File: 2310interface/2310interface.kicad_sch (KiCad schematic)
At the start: 63 parts, among them J4 Screw_Terminal_01x04, K1 Relay_SPDT, Q1 Q_NMOS_DSG, Q2 2N3904, SW1 SW_SPDT, U1 LD1117S50TR_SOT223

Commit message: Update after testing
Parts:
- C1: value C -> 100nF
- C2: value C -> 10uF
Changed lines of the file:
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@@
   )
   (symbol (lib_id "Device:R_US") (at 125.73 130.81 0) (unit 1)
-    (in_bom yes) (on_board yes) (dnp no) (fields_autoplaced)
-    (property "Reference" "R4" (at 128.27 129.54 0)
-      (effects (font (size 1.27 1.27)) (justify left))
-    )
-    (property "Value" "47K" (at 128.27 132.08 0)
+    (in_bom yes) (on_board yes) (dnp no)
+    (property "Reference" "R4" (at 121.92 130.81 0)
+      (effects (font (size 1.27 1.27)) (justify left))
+    )
+    (property "Value" "47K" (at 120.65 133.35 0)
       (effects (font (size 1.27 1.27)) (justify left))
     )
@@
       (effects (font (size 1.27 1.27)))
     )
-    (property "Value" "C" (at 194.31 88.9 90)
+    (property "Value" "10uF" (at 194.31 88.9 90)
       (effects (font (size 1.27 1.27)))
     )
@@
       (effects (font (size 1.27 1.27)))
     )
-    (property "Value" "C" (at 182.88 88.9 90)
-      (effects (font (size 1.27 1.27)))
-    )
+    (property "Value" "100nF" (at 182.88 88.9 90)
+      (effects (font (size 1.27 1.27)))
+    )

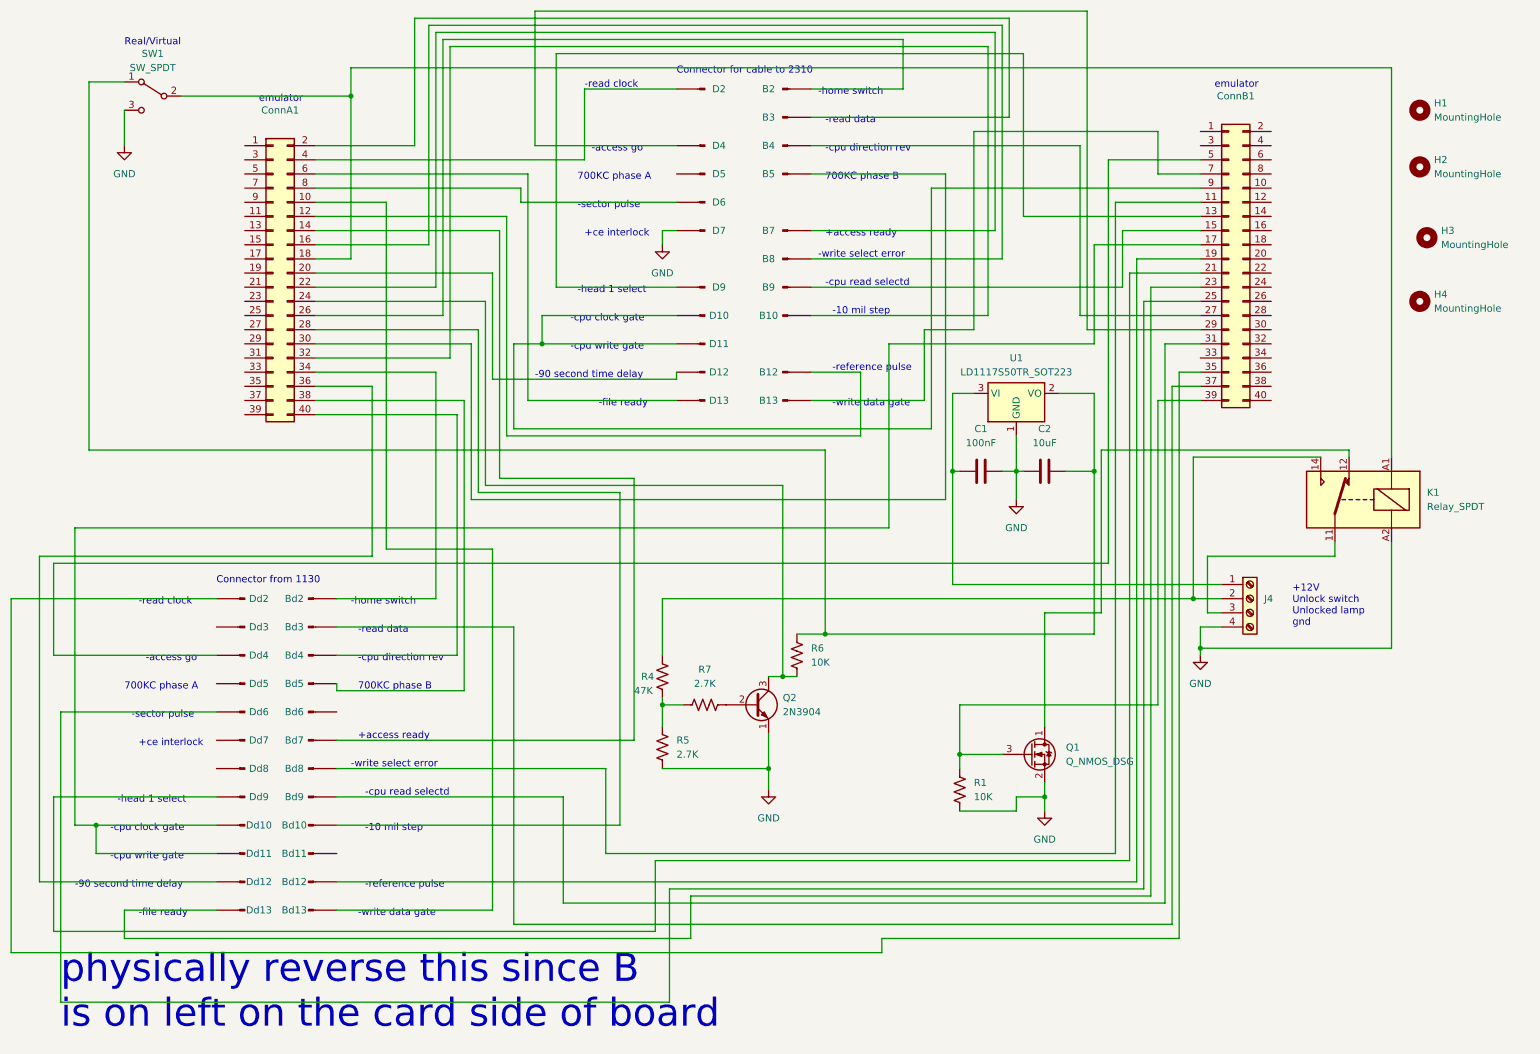
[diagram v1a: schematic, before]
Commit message: Fix defect in board
Inadvertent connection of +12V to the Unlock lamp driver
also increased current capacity for Unlock lamp traces
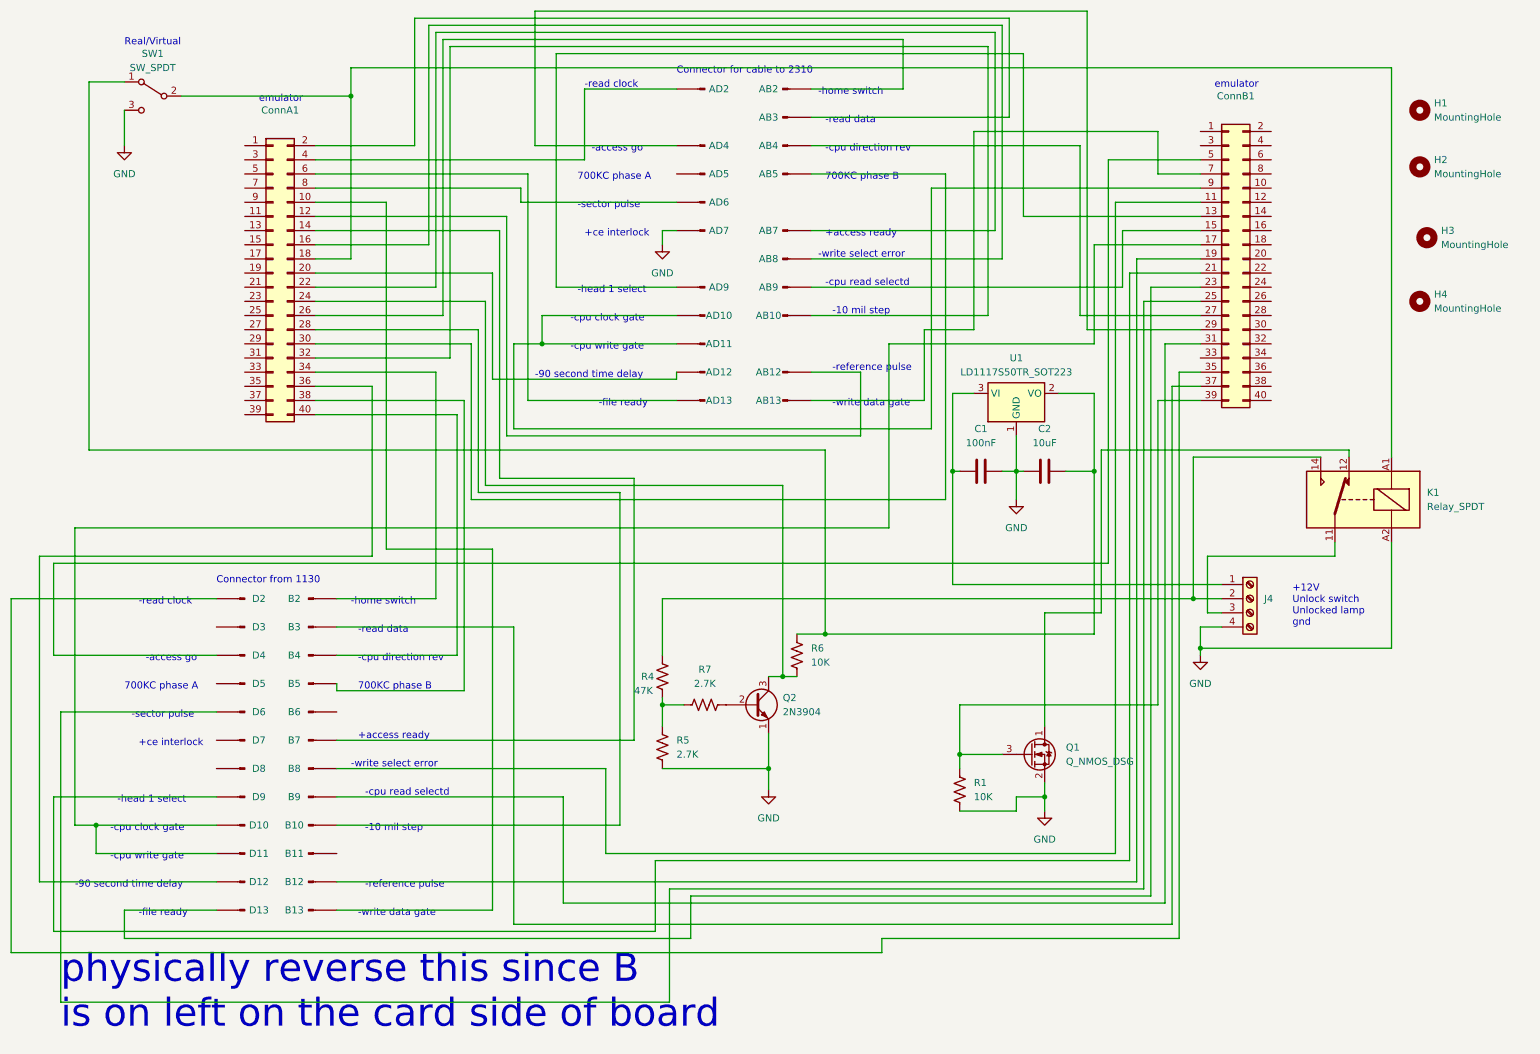
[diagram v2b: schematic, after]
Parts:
- renumbered B10 to AB10, B12 to AB12, B13 to AB13, B2 to AB2, B3 to AB3, B4 to AB4, B5 to AB5, B7 to AB7, B8 to AB8, B9 to AB9, D10 to AD10, D11 to AD11, D12 to AD12, D13 to AD13, D2 to AD2, D4 to AD4, D5 to AD5, D6 to AD6, D7 to AD7, D9 to AD9, Bd10 to B10, Bd11 to B11, Bd12 to B12, Bd13 to B13, Bd2 to B2, Bd3 to B3, Bd4 to B4, Bd5 to B5, Bd6 to B6, Bd7 to B7, Bd8 to B8, Bd9 to B9, Dd10 to D10, Dd11 to D11, Dd12 to D12, Dd13 to D13, Dd2 to D2, Dd3 to D3, Dd4 to D4, Dd5 to D5, Dd6 to D6, Dd7 to D7, Dd8 to D8, Dd9 to D9
